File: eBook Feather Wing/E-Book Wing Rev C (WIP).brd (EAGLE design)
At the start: 77.5 x 112.3 mm, 98 parts, among them IC1 MCP23008/SO, IC2 23K256-I/SN, J1 MJ-3523-SMT, Q1 IRLML0100, SW1 SPDT_SWITCH

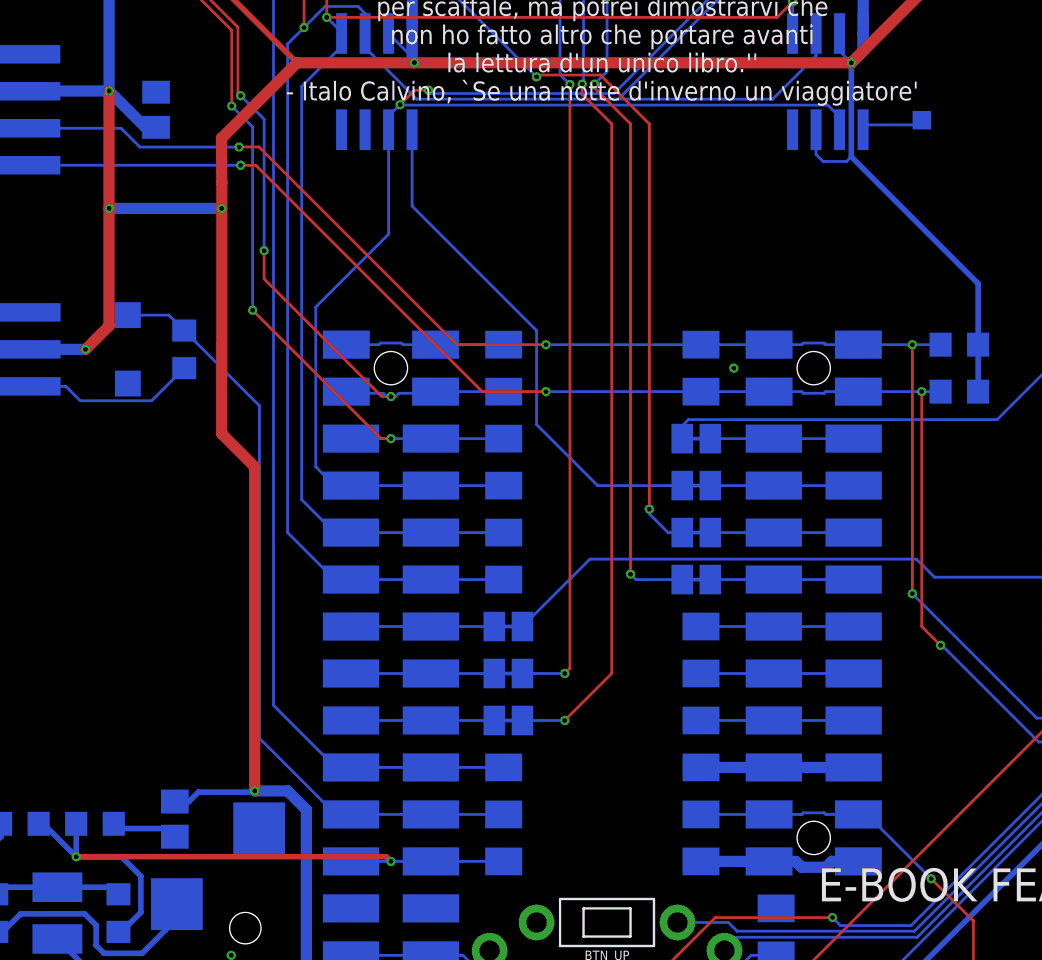
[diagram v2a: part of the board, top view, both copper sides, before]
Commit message: wire FCS to M4's 'extra' pin
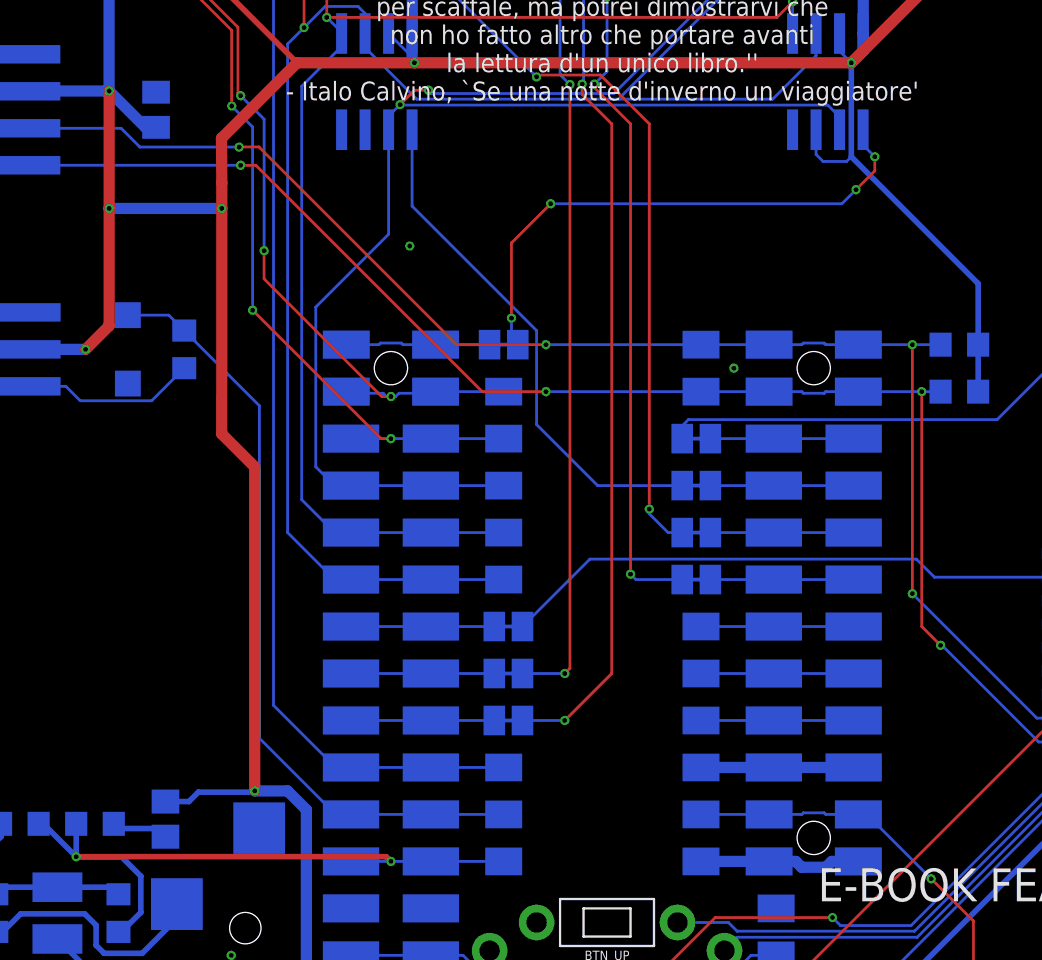
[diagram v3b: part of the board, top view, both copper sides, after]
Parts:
- removed XTRA: (no value), Adafruit 3.5in 480x320 FeatherWing:MICROBUILDER_PAD-1.5X2.0
- FCS: device Adafruit 3.5in 480x320 FeatherWing:MICROBUILDER_TESTPOINT_PAD_1MM -> Adafruit 3.5in 480x320 FeatherWing:MICROBUILDER_SOLDERJUMPER_CLOSEDWIRE
- moved FCS 25.7 mm to (33.3, 44.5)
- moved FB1 0.51 mm to (15.0, 18.8)
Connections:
- net FLASH_CS: now also FCS.2; no longer FCS.P$1
- net NC_D4: now also FCS.1; no longer XTRA.P$1
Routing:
- net FLASH_CS: track 3.39 -> 29.4 mm, vias 0 -> 4
- net NC_D4: track 8.58 -> 7.82 mm
- net AVCC: track 3.74 -> 3.23 mm
- net +3V3: track 368.9 -> 369.4 mm
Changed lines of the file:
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@@
 <layer number="27" name="tValues" color="7" fill="1" visible="no" active="yes"/>
 <layer number="28" name="bValues" color="7" fill="1" visible="no" active="yes"/>
-<layer number="29" name="tStop" color="7" fill="3" visible="yes" active="yes"/>
+<layer number="29" name="tStop" color="7" fill="3" visible="no" active="yes"/>
 <layer number="30" name="bStop" color="7" fill="6" visible="no" active="yes"/>
 <layer number="31" name="tCream" color="7" fill="4" visible="no" active="yes"/>
@@
 <attribute name="VALUE" x="3.81" y="16.764" size="0.508" layer="28" font="vector" ratio="18" rot="MR270" align="center"/>
 </element>
-<element name="FB1" library="microbuilder" package="0805" value="FERRITE" x="15.494" y="18.796" smashed="yes" rot="MR90">
-<attribute name="NAME" x="15.494" y="16.383" size="0.508" layer="26" font="vector" ratio="18" rot="MR0" align="center"/>
-<attribute name="VALUE" x="14.732" y="20.828" size="0.508" layer="28" font="vector" ratio="18" rot="MR90" align="center"/>
+<element name="FB1" library="microbuilder" package="0805" value="FERRITE" x="14.986" y="18.796" smashed="yes" rot="MR90">
+<attribute name="NAME" x="14.986" y="16.383" size="0.508" layer="26" font="vector" ratio="18" rot="MR0" align="center"/>
+<attribute name="VALUE" x="14.224" y="20.828" size="0.508" layer="28" font="vector" ratio="18" rot="MR90" align="center"/>
 </element>
 <element name="A2_PORT" library="microbuilder" package="JSTPH3" value="JST PH 3" x="4.318" y="70.104" smashed="yes" rot="MR270">
@@
 <attribute name="NAME" x="35.052" y="41.826" size="0.508" layer="26" font="vector" ratio="18" rot="MR270" align="center"/>
 <attribute name="VALUE" x="33.974" y="40.81" size="0.4064" layer="28" ratio="10" rot="MR270"/>
-</element>
-<element name="XTRA" library="Adafruit 3.5in 480x320 FeatherWing" package="MICROBUILDER_PAD-1.5X2.0" value="" x="33.274" y="44.45" smashed="yes" rot="MR270">
-<attribute name="NAME" x="35.052" y="44.366" size="0.508" layer="26" font="vector" ratio="18" rot="MR270" align="center"/>
-<attribute name="VALUE" x="33.974" y="43.35" size="0.4064" layer="28" ratio="10" rot="MR270"/>
 </element>
 <element name="3V" library="Adafruit 3.5in 480x320 FeatherWing" package="MICROBUILDER_PAD-1.5X2.0" value="" x="48.006" y="8.89" smashed="yes" rot="MR270">
@@
 <attribute name="NAME" x="35.814" y="24.257" size="0.508" layer="26" font="vector" ratio="18" rot="MR90" align="center"/>
 <attribute name="VALUE" x="32.004" y="25.781" size="0.4064" layer="28" ratio="10" rot="MR180"/>
-</element>
-<element name="FCS" library="Adafruit 3.5in 480x320 FeatherWing" package="MICROBUILDER_TESTPOINT_PAD_1MM" value="" x="55.88" y="56.58611875" smashed="yes" rot="MR180">
-<attribute name="NAME" x="55.88" y="55.31611875" size="0.508" layer="26" font="vector" ratio="18" rot="MR180" align="center"/>
-<attribute name="VALUE" x="56.98" y="57.28611875" size="0.4064" layer="28" ratio="10" rot="MR180"/>
 </element>
 <element name="BTN_RIGHT" library="My Stuff" package="MJTP1250" value="MJTP1250_SPST_SWITCH" x="45.212" y="9.144" smashed="yes" rot="R270"/>
@@
 <element name="SW1" library="My Stuff" package="A10767" value="SPDT_SWITCH" x="58.674" y="4.826" smashed="yes" rot="MR0">
 <attribute name="NAME" x="58.674" y="7.747" size="0.8128" layer="52" font="vector" ratio="18" rot="MR0" align="center"/>
+</element>
+<element name="FCS" library="Adafruit 3.5in 480x320 FeatherWing" package="MICROBUILDER_SOLDERJUMPER_CLOSEDWIRE" value="" x="33.274" y="44.45" smashed="yes" rot="MR180">
+<attribute name="NAME" x="35.56" y="44.45" size="0.508" layer="26" font="vector" ratio="18" rot="MR90" align="center"/>
+<attribute name="VALUE" x="31.75" y="46.101" size="0.4064" layer="28" ratio="10" rot="MR180"/>
 </element>
 </elements>
@@
 <via x="61.722" y="106.68" extent="1-16" drill="0.254"/>
 <contactref element="SW1" pad="P$3"/>
+<via x="28.194" y="49.784" extent="1-16" drill="0.254"/>
 </signal>
 <signal name="SD_CS">
@@
 <contactref element="MS1" pad="16'"/>
 <contactref element="MS1" pad="16"/>
-<contactref element="XTRA" pad="P$1"/>
 <wire x1="24.765" y1="44.45" x2="26.528625" y2="44.45" width="0.1524" layer="16"/>
 <wire x1="26.528625" y1="44.45" x2="26.615825" y2="44.5372" width="0.1524" layer="16"/>
@@
 <wire x1="27.740175" y1="44.5372" x2="27.827375" y2="44.45" width="0.1524" layer="16"/>
 <wire x1="27.827375" y1="44.45" x2="29.591" y2="44.45" width="0.1524" layer="16"/>
-<wire x1="29.591" y1="44.45" x2="33.274" y2="44.45" width="0.1524" layer="16"/>
+<contactref element="FCS" pad="1"/>
+<wire x1="29.591" y1="44.45" x2="32.512" y2="44.45" width="0.1524" layer="16"/>
 </signal>
 <signal name="+3V3">
@@
 <wire x1="68.722" y1="76.342" x2="70.1802" y2="76.342" width="0.6096" layer="1"/>
 <wire x1="52.07" y1="59.69" x2="68.722" y2="76.342" width="0.6096" layer="1"/>
-<wire x1="15.494" y1="19.746" x2="16.256" y2="19.746" width="0.3048" layer="16"/>
+<wire x1="14.986" y1="19.746" x2="16.256" y2="19.746" width="0.3048" layer="16"/>
 <wire x1="16.256" y1="19.746" x2="16.764" y2="20.254" width="0.3048" layer="16"/>
 </signal>
@@
 <contactref element="R6" pad="1"/>
 <contactref element="FB1" pad="1"/>
-<wire x1="15.494" y1="17.846" x2="15.052" y2="18.288" width="0.3048" layer="16"/>
-<wire x1="15.052" y1="18.288" x2="12.192" y2="18.288" width="0.3048" layer="16"/>
+<wire x1="14.986" y1="17.846" x2="14.544" y2="18.288" width="0.3048" layer="16"/>
+<wire x1="14.544" y1="18.288" x2="12.192" y2="18.288" width="0.3048" layer="16"/>
 <wire x1="12.192" y1="18.288" x2="12.192" y2="18.542" width="0.3048" layer="16"/>
 </signal>
@@
 <signal name="FLASH_CS">
 <contactref element="IC3" pad="1"/>
-<contactref element="FCS" pad="P$1"/>
-<wire x1="55.88" y1="56.58611875" x2="55.626" y2="56.33211875" width="0.1524" layer="16"/>
-<wire x1="55.626" y1="56.33211875" x2="52.96311875" y2="56.33211875" width="0.1524" layer="16"/>
-<wire x1="52.96311875" y1="56.33211875" x2="52.705" y2="56.074" width="0.1524" layer="16"/>
+<contactref element="FCS" pad="2"/>
+<wire x1="34.036" y1="44.45" x2="33.69475" y2="44.79125" width="0.1524" layer="16"/>
+<wire x1="33.69475" y1="44.79125" x2="33.69475" y2="45.88675" width="0.1524" layer="16"/>
+<via x="33.69475" y="45.88675" extent="1-16" drill="0.254"/>
+<wire x1="33.69475" y1="45.88675" x2="33.69475" y2="49.95075" width="0.1524" layer="1"/>
+<wire x1="33.69475" y1="49.95075" x2="35.814" y2="52.07" width="0.1524" layer="1"/>
+<via x="35.814" y="52.07" extent="1-16" drill="0.254"/>
+<wire x1="35.814" y1="52.07" x2="51.562" y2="52.07" width="0.1524" layer="16"/>
+<wire x1="51.562" y1="52.07" x2="52.324" y2="52.832" width="0.1524" layer="16"/>
+<via x="52.324" y="52.832" extent="1-16" drill="0.254"/>
+<wire x1="52.324" y1="52.832" x2="53.34" y2="53.848" width="0.1524" layer="1"/>
+<wire x1="53.34" y1="53.848" x2="53.34" y2="54.61" width="0.1524" layer="1"/>
+<via x="53.34" y="54.61" extent="1-16" drill="0.254"/>
+<wire x1="53.34" y1="54.61" x2="52.705" y2="55.245" width="0.1524" layer="16"/>
+<wire x1="52.705" y1="55.245" x2="52.705" y2="56.074" width="0.1524" layer="16"/>
 </signal>
 <signal name="GPIO_INT">

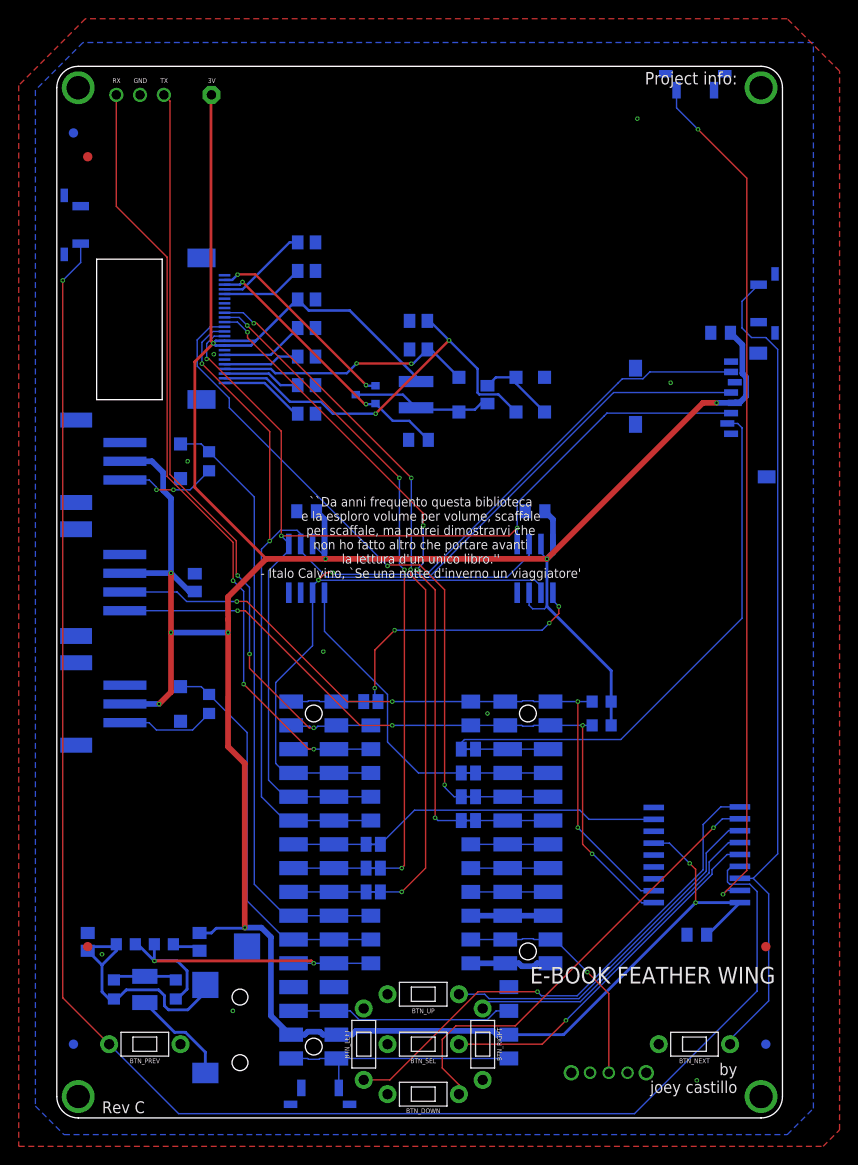
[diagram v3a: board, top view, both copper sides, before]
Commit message: silkscreen adjustments to ebook wing rev 3
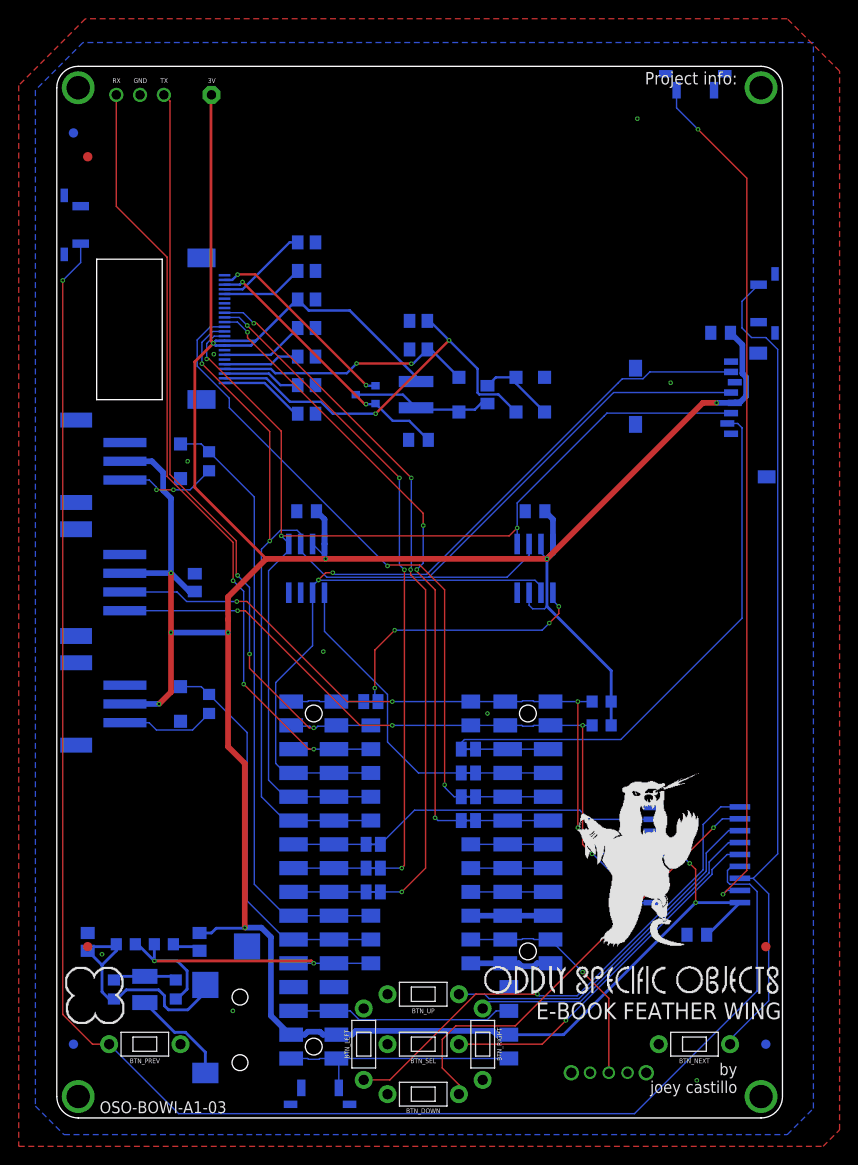
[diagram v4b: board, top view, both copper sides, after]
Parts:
- added U$44: OSO_GRAPHIC, My Stuff:OSO_GRAPHIC
- added U$45: OSO_BEAR, My Stuff:OSO_BEAR_750MIL
- added U$48: OSO_TEXTOSO_TEXT_ONELINE_125MIL, My Stuff:OSO_ONELINE_125MIL
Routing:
- net BTN_PREV: track 182.9 -> 184.0 mm
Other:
- board text added: "OSO-BOWI-A1-03"
- board text removed: "Rev C"
- board text removed: "``Da anni frequento questa biblioteca e la esploro volume per volume, scaffale per scaffale, ma potrei dimostrarvi che non ho fatto altro che portare avanti la lettura d'un unico libro.'' - Italo Calvino, `Se una notte d'inverno un viaggiatore'"
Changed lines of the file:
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@@
 <layer number="27" name="tValues" color="7" fill="1" visible="no" active="yes"/>
 <layer number="28" name="bValues" color="7" fill="1" visible="no" active="yes"/>
-<layer number="29" name="tStop" color="7" fill="3" visible="no" active="yes"/>
+<layer number="29" name="tStop" color="7" fill="3" visible="yes" active="yes"/>
 <layer number="30" name="bStop" color="7" fill="6" visible="no" active="yes"/>
 <layer number="31" name="tCream" color="7" fill="4" visible="no" active="yes"/>
@@
 spare, omit this chip (and C4).</text>
 <wire x1="55.626" y1="53.086" x2="46.736" y2="53.086" width="0.1524" layer="22" style="shortdash"/>
-<text x="76.454" y="16.129" size="1.778" layer="21" font="vector" ratio="18" distance="20" align="top-right">E-BOOK FEATHER WING</text>
+<text x="77.089" y="12.319" size="1.778" layer="21" font="vector" ratio="18" distance="20" align="top-right">E-BOOK FEATHER WING</text>
 <text x="57.912" y="106.172" size="1.27" layer="22" font="vector" ratio="18" rot="MR0" align="top-left">E-PAPER DISPLAY</text>
 <text x="57.912" y="104.394" size="0.8128" layer="22" font="vector" rot="MR0" align="top-left">&gt;1 NC
@@
 <text x="71.374" y="25.908" size="0.508" layer="22" font="vector" rot="MR0" align="top-left">BTN_NEXT</text>
 <text x="71.374" y="24.638" size="0.508" layer="22" font="vector" rot="MR0" align="top-left">BTN_LOCK</text>
-<text x="38.608" y="61.976" size="1.016" layer="21" font="vector" align="center">``Da anni frequento questa biblioteca
-e la esploro volume per volume, scaffale
-per scaffale, ma potrei dimostrarvi che
-non ho fatto altro che portare avanti
-la lettura d'un unico libro.''
-- Italo Calvino, `Se una notte d'inverno un viaggiatore'</text>
 <text x="27.7622" y="3.937" size="0.508" layer="22" font="vector" ratio="18" rot="MR180" align="center">RESET</text>
-<text x="4.572" y="0.508" size="1.27" layer="21" font="vector">Rev C</text>
+<text x="4.318" y="0.508" size="1.27" layer="21" font="vector" ratio="18">OSO-BOWI-A1-03</text>
 <text x="10.033" y="42.1894" size="0.508" layer="22" font="vector" ratio="18" rot="MR90" align="center">A1</text>
 <text x="10.033" y="44.1706" size="0.508" layer="22" font="vector" ratio="18" rot="MR90" align="center">3V</text>
@@
 <text x="68.072" y="1.27" size="0.8128" layer="22" font="vector" rot="MR0" align="top-center">CC-BY-SA 4.0</text>
 <text x="72.39" y="2.032" size="1.27" layer="29" font="vector" ratio="18" align="top-right">@josecastillo</text>
-<wire x1="55.626" y1="-9.652" x2="34.29" y2="-9.652" width="0.0508" layer="22"/>
 <text x="22.098" y="36.068" size="0.8128" layer="22" font="vector" rot="MR0" align="top-left">The DAC on A0 drives mono
 headphone jack J1. FB1 &amp; FB2
@@
 <attribute name="VALUE" x="31.75" y="46.101" size="0.4064" layer="28" ratio="10" rot="MR180"/>
 </element>
+<element name="U$48" library="My Stuff" package="OSO_ONELINE_125MIL" value="OSO_TEXTOSO_TEXT_ONELINE_125MIL" x="45.339" y="14.732" smashed="yes"/>
+<element name="U$44" library="My Stuff" package="OSO_GRAPHIC" value="OSO_GRAPHIC" x="3.81" y="13.081" smashed="yes"/>
+<element name="U$45" library="My Stuff" package="OSO_BEAR_750MIL" value="OSO_BEAR" x="61.976" y="27.178" smashed="yes"/>
 </elements>
 <signals>
@@
 <wire x1="49.388625" y1="19.05" x2="47.625" y2="19.05" width="0.1524" layer="16"/>
 <wire x1="47.625" y1="19.05" x2="43.942" y2="19.05" width="0.1524" layer="16"/>
-<via x="56.388" y="15.5702" extent="1-16" drill="0.254"/>
-<wire x1="56.388" y1="15.5702" x2="52.9082" y2="19.05" width="0.1524" layer="16"/>
-<wire x1="52.9082" y1="19.05" x2="52.451" y2="19.05" width="0.1524" layer="16"/>
-<wire x1="56.388" y1="15.5702" x2="58.674" y2="13.2842" width="0.1524" layer="1"/>
+<via x="55.88" y="15.5702" extent="1-16" drill="0.254"/>
+<wire x1="52.451" y1="19.05" x2="52.451" y2="18.9992" width="0.1524" layer="16"/>
+<wire x1="55.88" y1="15.5702" x2="52.451" y2="18.9992" width="0.1524" layer="16"/>
+<wire x1="55.88" y1="15.5702" x2="58.674" y2="12.7762" width="0.1524" layer="1"/>
 <contactref element="SW1" pad="P$2"/>
-<wire x1="58.674" y1="13.2842" x2="58.674" y2="4.826" width="0.1524" layer="1"/>
+<wire x1="58.674" y1="12.7762" x2="58.674" y2="4.826" width="0.1524" layer="1"/>
 </signal>
 <signal name="AREF">
@@
 <wire x1="2.2956" y1="91.3226" x2="0.381" y2="89.408" width="0.1524" layer="16"/>
 <via x="0.381" y="89.408" extent="1-16" drill="0.254"/>
-<wire x1="0.381" y1="89.408" x2="0.381" y2="12.827" width="0.1524" layer="1"/>
-<wire x1="5.334" y1="7.874" x2="0.381" y2="12.827" width="0.1524" layer="1"/>
+<wire x1="0.381" y1="89.408" x2="0.381" y2="11.049" width="0.1524" layer="1"/>
+<wire x1="5.334" y1="7.874" x2="3.556" y2="7.874" width="0.1524" layer="1"/>
+<wire x1="3.556" y1="7.874" x2="0.381" y2="11.049" width="0.1524" layer="1"/>
 <wire x1="5.334" y1="7.874" x2="12.7508" y2="0.4572" width="0.1524" layer="16"/>
 <wire x1="12.7508" y1="0.4572" x2="61.4172" y2="0.4572" width="0.1524" layer="16"/>
@@
 <contactref element="IC1" pad="10"/>
 <contactref element="BTN_LEFT" pad="P$1"/>
-<wire x1="51.054" y1="13.474" x2="51.4858" y2="13.0422" width="0.1524" layer="16"/>
-<wire x1="55.3012" y1="13.0422" x2="51.4858" y2="13.0422" width="0.1524" layer="16"/>
-<via x="51.054" y="13.474" extent="1-16" drill="0.254"/>
-<wire x1="51.054" y1="13.474" x2="44.716" y2="13.474" width="0.1524" layer="1"/>
+<wire x1="51.054" y1="13.22" x2="51.2318" y2="13.0422" width="0.1524" layer="16"/>
+<wire x1="55.3012" y1="13.0422" x2="51.2318" y2="13.0422" width="0.1524" layer="16"/>
+<via x="51.054" y="13.22" extent="1-16" drill="0.254"/>
+<wire x1="51.054" y1="13.22" x2="44.462" y2="13.22" width="0.1524" layer="1"/>
 <wire x1="35.306" y1="4.064" x2="32.512" y2="4.064" width="0.1524" layer="1"/>
-<wire x1="44.716" y1="13.474" x2="35.306" y2="4.064" width="0.1524" layer="1"/>
+<wire x1="44.462" y1="13.22" x2="35.306" y2="4.064" width="0.1524" layer="1"/>
 <wire x1="68.74675" y1="31.32925" x2="68.74675" y2="26.48775" width="0.1524" layer="16"/>
 <wire x1="55.3012" y1="13.0422" x2="68.74675" y2="26.48775" width="0.1524" layer="16"/>
